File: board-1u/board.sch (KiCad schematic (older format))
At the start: 38 parts, among them J1 Power, J10 B3, J11 B4, J2 A, J3 A1, J4 A2, J5 A3, J6 A4, J7 B, J8 B1, J9 B2, U1 OPA4991, U2 OPA4991, U3 LM358

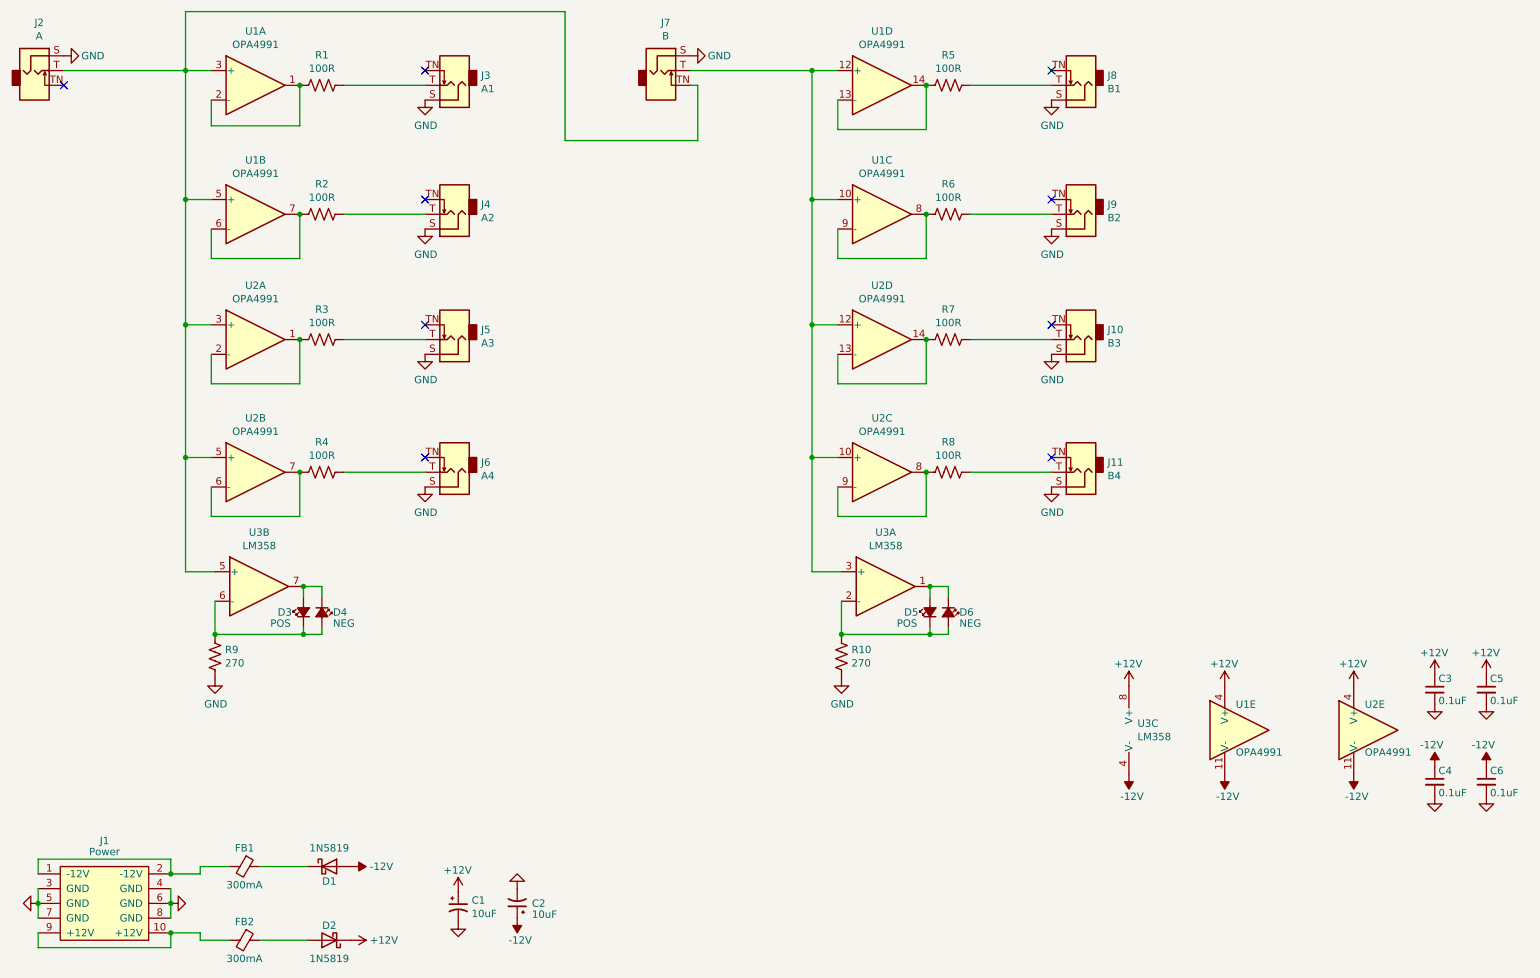
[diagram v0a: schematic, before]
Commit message: Changes from tests on first revision
1. Silkscreen legibility changes
2. Added version numbers and such to page info blocks
3. Change MPNs and values
4. Change footprints for LEDs and Diodes.
5. Pin one markers
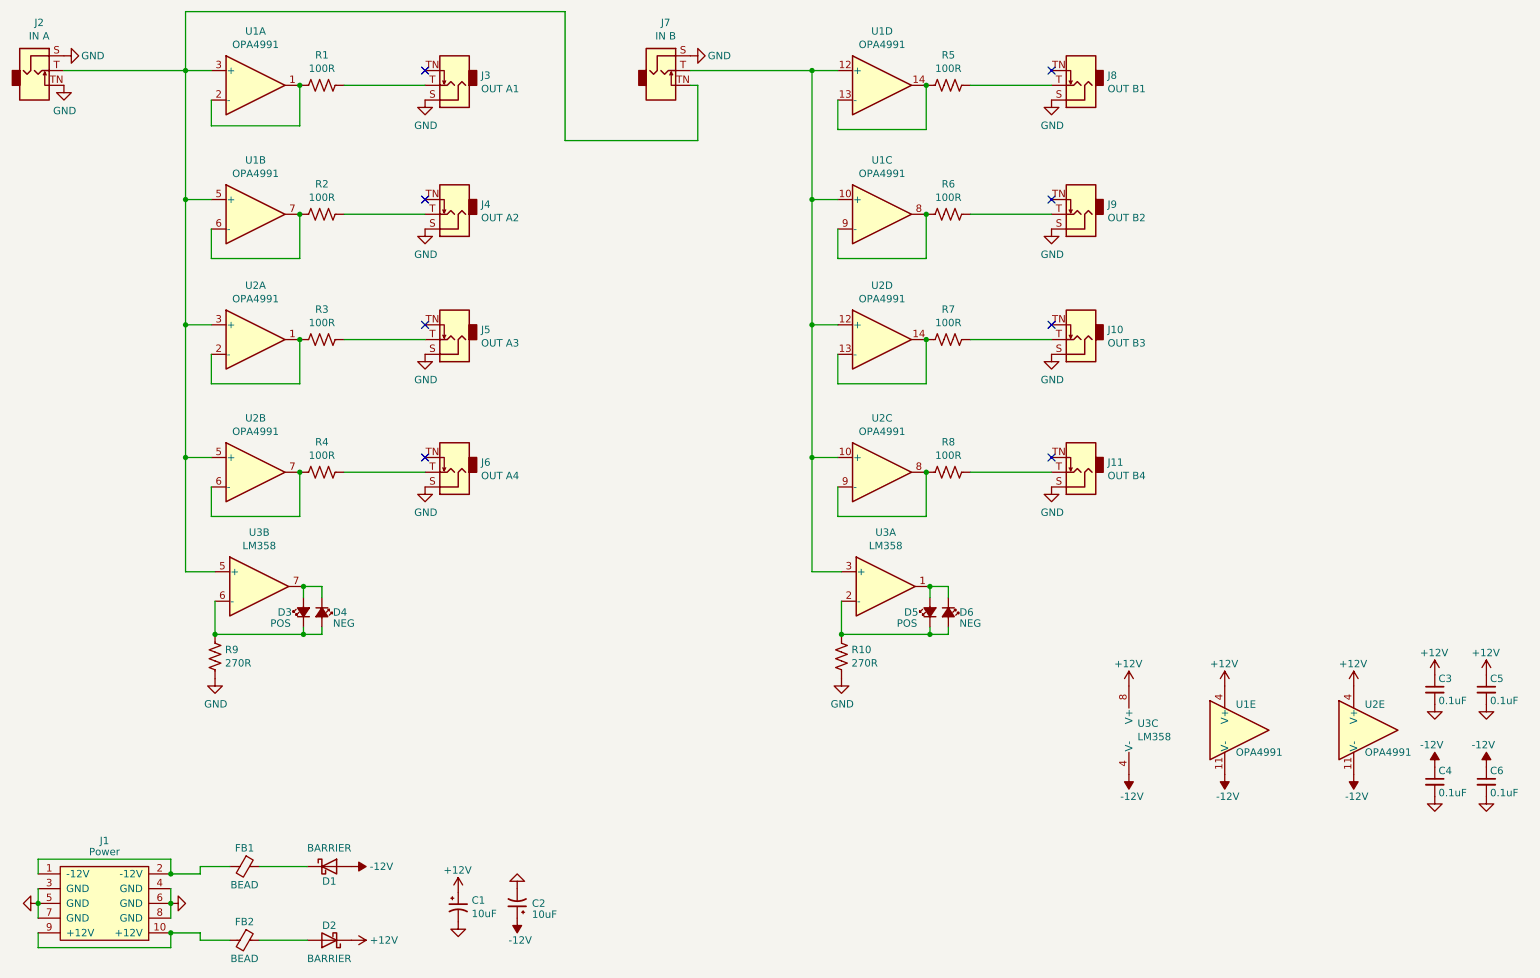
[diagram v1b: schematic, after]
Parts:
- C1, C2: Notes (none) -> 0805, 25V+, 10%, Bulk cap; unit cost 0.17 -> (none)
- C3, C4, C5, C6: Notes (none) -> 0603, 25V+, 10%, Bypass cap; unit cost 0.03 -> (none)
- D1, D2: value 1N5819 -> BARRIER; footprint Diode_SMD:D_SOD-323_HandSoldering -> winterbloom:DIODE_SOD-123_SOD-123F; Notes (none) -> Any PMEGxxxxEGW part, 500mA If; mpn PMEG4010EGWX -> PMEG2005EGWX; unit cost 0.22 -> (none)
- D3, D5: footprint LED_SMD:LED_0805_2012Metric_Pad1.15x1.40mm_HandSolder -> winterbloom:LED_0805_Kingbright_APT2012; Notes (none) -> APT2012VBC/D; unit cost 0.24 -> (none)
- D4, D6: footprint LED_SMD:LED_0805_2012Metric_Pad1.15x1.40mm_HandSolder -> winterbloom:LED_0805_Kingbright_APT2012; Notes (none) -> APT2012SURCK; unit cost 0.17 -> (none)
- FB1, FB2: value 300mA -> BEAD; Notes (none) -> 300mA; unit cost 0.13 -> (none)
- J10: value B3 -> OUT B3
- J11: value B4 -> OUT B4
- J2: value A -> IN A
- J3: value A1 -> OUT A1
- J4: value A2 -> OUT A2
- J5: value A3 -> OUT A3
- J6: value A4 -> OUT A4
- J7: value B -> IN B
- J8: value B1 -> OUT B1
- J9: value B2 -> OUT B2
- R1, R2, R3, R4, R5, R6, R7, R8: Notes (none) -> thin film; mpn MCT06030C1001FP500 -> R0816P-101-D
- R10, R9: value 270 -> 270R; Notes (none) -> 5%, thick film; mpn ERA-3AED271V -> ERJ-3GEYJ271V; unit cost 0.06 -> (none)
- U1, U2: unit cost 2.55 -> (none)
- U3: unit cost 0.41 -> (none)
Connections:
- net GND: now also J2.TN (Tip_normalize)
- no-connect marks 9 -> 8
